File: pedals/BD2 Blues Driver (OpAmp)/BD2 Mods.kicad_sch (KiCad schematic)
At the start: 67 parts, among them J1 +9v, J3 PCB, Q1 BC547B, Q2 BC547, U1 TL072, U2 TL074

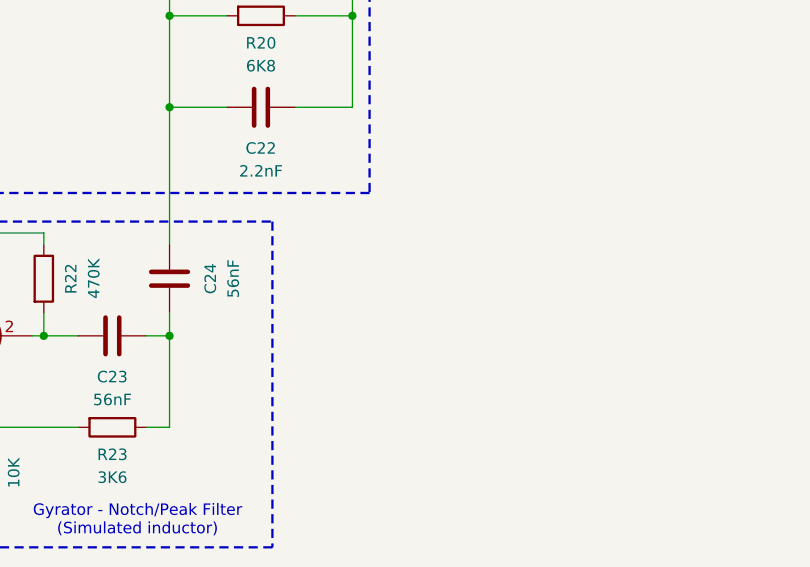
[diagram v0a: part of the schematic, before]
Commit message: Cap change in the gyrator
56nF caps are hard to find now, so added an alternative of 47nF or 68nF
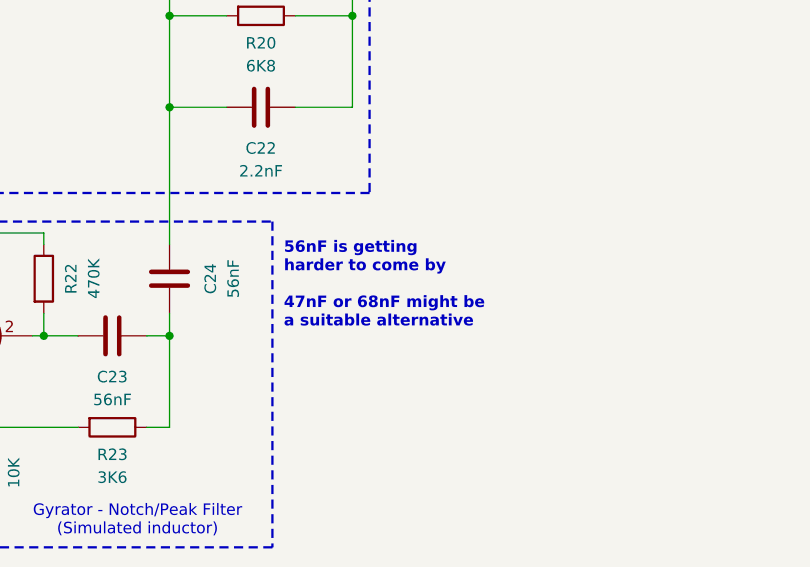
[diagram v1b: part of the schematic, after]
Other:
- note added: "56nF is getting harder to come by 47nF or 68nF might be a suitable alternative"
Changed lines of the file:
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@@
+		)
+	)
+	(text "56nF is getting\nharder to come by\n\n47nF or 68nF might be\na suitable alternative"
+		(exclude_from_sim no)
+		(at 200.66 181.102 0)
+		(effects
+			(font
+				(size 1.27 1.27)
+				(thickness 0.254)
+				(bold yes)
+				(color 191 111 0 1)
+			)
+			(justify left)
 		)
 	)
